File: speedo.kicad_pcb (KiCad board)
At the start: 4 copper layers, 70 x 34 mm, 52 parts, among them J1 Conn_01x08, J2 Conn_01x10, J3 Prog Header, Q1 BSS138, SW1 SW_Push, U1 US1881, U2 LT1762-3.3, U3 4N25, U4 LT1762-5, U5 ATMEGA328P-AU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

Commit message: Moved some pins around
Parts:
- renumbered REF** to REF1, REF** to REF2
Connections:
- U5 pad 1: BUTTON2 -> BUTTON1
- U5 pad 12: Net-(U5-Pad12) -> TACH
- U5 pad 2: TACH -> BUTTON2
- U5 pad 32: BUTTON1 -> HALL-EFF
- U5 pad 9: HALL-EFF -> Net-(U5-Pad9)
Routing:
- net HALL-EFF: track 56.0 -> 17.2 mm, vias 2 -> 0
- net BUTTON1: track 56.6 -> 60.1 mm
- net TACH: track 48.3 -> 45.3 mm
- net BUTTON2: track 60.7 -> 63.4 mm

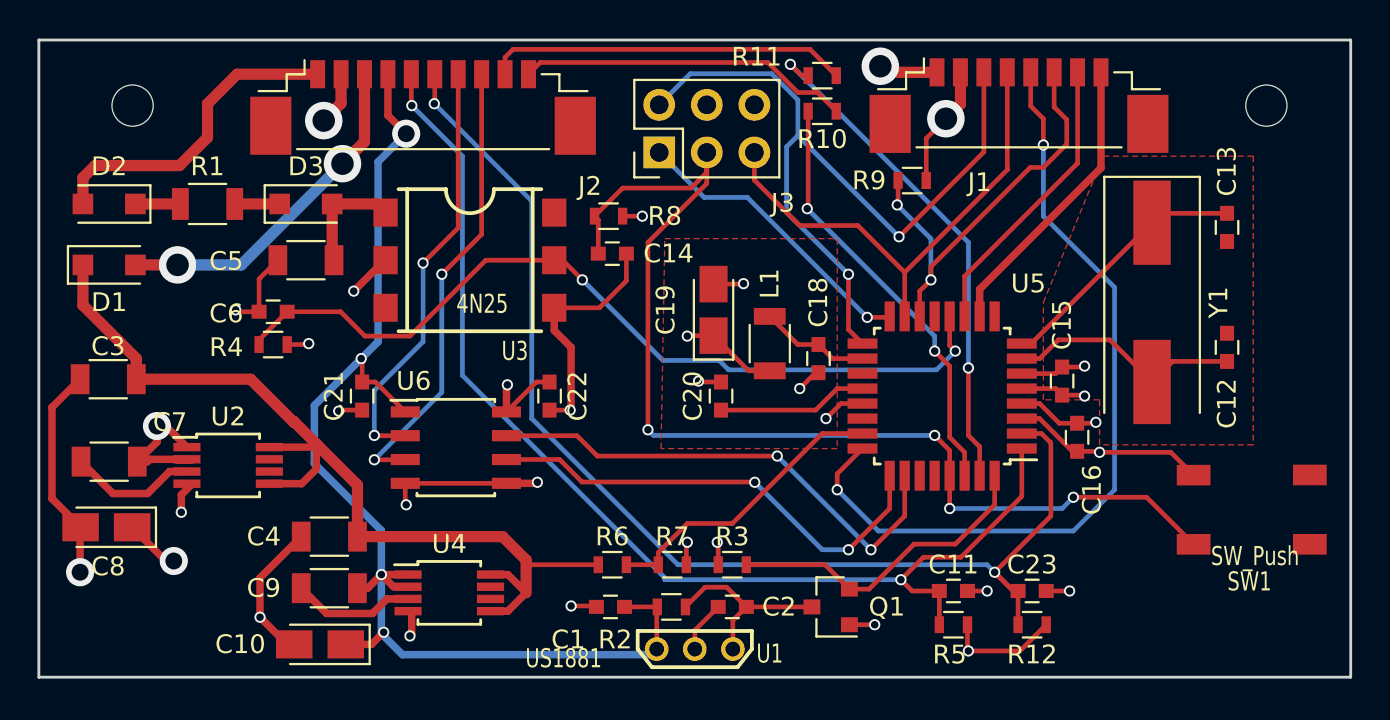
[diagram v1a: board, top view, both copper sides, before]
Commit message: Merged atmega644
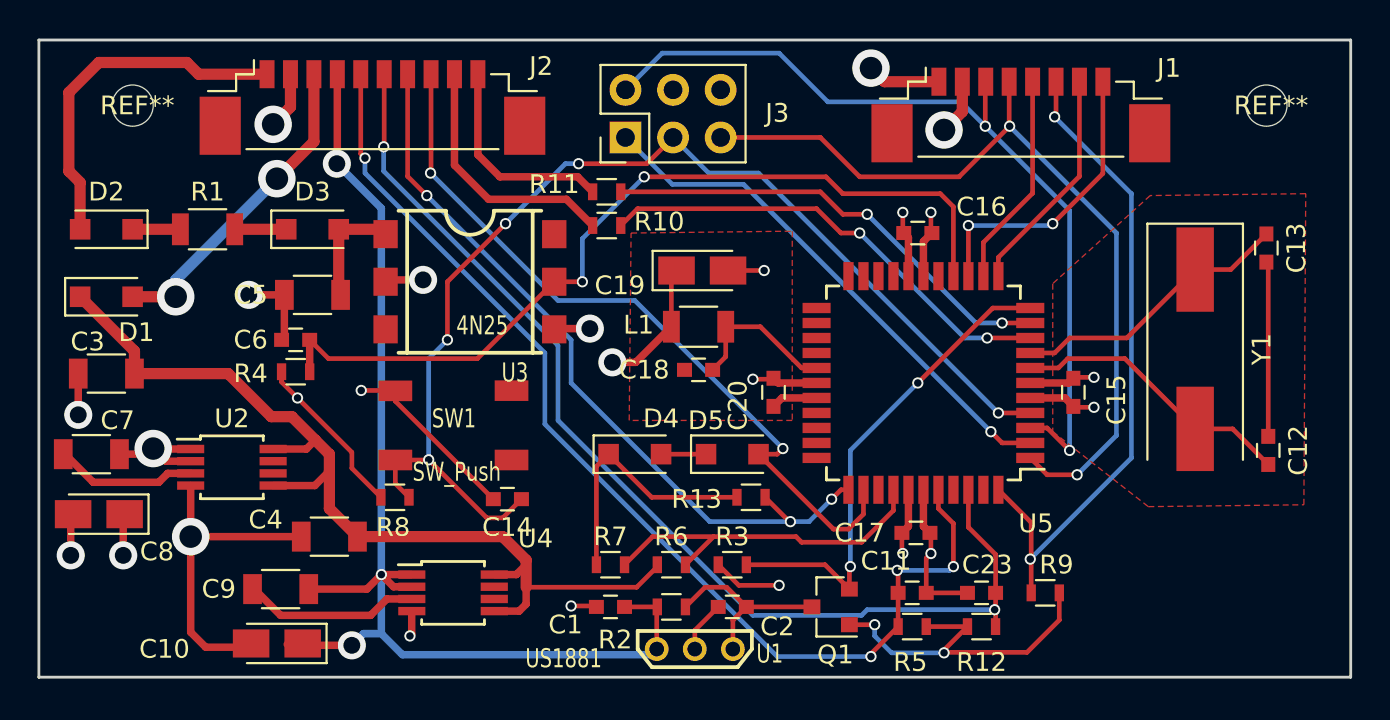
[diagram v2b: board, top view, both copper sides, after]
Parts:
- removed C21, C22: 100nF, Capacitors_SMD:C_0603
- removed U6: ADuM1200BR, Housings_SOIC:SOIC-8_3.9x4.9mm_Pitch1.27mm
- added C17: 100nF, Capacitors_SMD:C_0603, F.Cu at (146.8, 128.3)
- added D4: D, Diodes_SMD:D_SOD-123F, F.Cu at (131.8, 124.1)
- added D5: D, Diodes_SMD:D_SOD-123F, F.Cu at (137.0, 124.1)
- added R13: 18K, Resistors_SMD:R_0603, F.Cu at (138.0, 126.4)
- U5: value ATMEGA328P-AU -> ATMEGA644-20AU; footprint Housings_QFP:TQFP-32_7x7mm_Pitch0.8mm -> Housings_QFP:TQFP-44_10x10mm_Pitch0.8mm
- Y1: value 10MHz 18pF -> 16MHz 18pF
- moved SW1 42.8 mm to (122.4, 122.7)
- moved R9 23.1 mm to (153.7, 131.5)
- moved R8 18.8 mm to (119.0, 126.4), turned to 0 degrees
- moved C14 14.2 mm to (125.0, 126.5), turned to 180 degrees
- moved C16 13.8 mm to (146.9, 112.3), turned to 180 degrees
- moved R11 13.1 mm to (130.3, 110.1), turned to 0 degrees
- moved R10 13.0 mm to (130.3, 111.9), turned to 0 degrees
- moved C18 6.43 mm to (135.2, 119.6), turned to 180 degrees
- moved C12 5.92 mm to (165.6, 123.9)
- moved L1 3.91 mm to (135.2, 117.3), turned to 0 degrees
- moved Y1 3.40 mm to (161.7, 118.5)
- moved R7 3.30 mm to (130.5, 130.0), turned to 0 degrees
- moved R6 3.15 mm to (133.8, 130.0)
- moved C20 2.81 mm to (139.2, 120.8)
- moved R12 2.70 mm to (150.3, 133.3), turned to 0 degrees
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- renumbered REF2 to REF**, REF1 to REF**
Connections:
- net /xtal1 renamed Net-(C12-Pad2)
- net /xtal2 renamed Net-(C13-Pad2)
- J2 pad 10: RX -> TX
- J2 pad 7: GPIO1 -> LM35-POS
- J2 pad 8: GPIO2 -> LM35-NEG
- J2 pad 9: TX -> RX
- L1 pad 1: Net-(C18-Pad1) -> +3V3
- L1 pad 2: +3V3 -> Net-(C18-Pad1)
- U5 pad 1: BUTTON1 -> MOSI
- U5 pad 10: LCD-LED -> Net-(R11-Pad2)
- U5 pad 11: LCD-RST -> HALL-EFF
- U5 pad 12: TACH -> LCD-RST
- U5 pad 13: Net-(U5-Pad13) -> LCD-DC
- U5 pad 14: LCD-CS -> LCD-LED
- U5 pad 15: MOSI -> TACH
- U5 pad 16: MISO -> Net-(U5-Pad16)
- U5 pad 17: SCK -> +3V3
- U5 pad 18: Net-(C18-Pad1) -> GND
- U5 pad 2: BUTTON2 -> MISO
- U5 pad 20: Net-(C20-Pad1) -> Net-(U5-Pad20)
- U5 pad 21: GND -> Net-(U5-Pad21)
- U5 pad 23: VMEAS -> Net-(U5-Pad23)
- U5 pad 24: LCD-DC -> Net-(U5-Pad24)
- U5 pad 25: GPIO2-ISO -> Net-(U5-Pad25)
- U5 pad 26: GPIO1-ISO -> Net-(U5-Pad26)
- U5 pad 27: Net-(U5-Pad27) -> Net-(C18-Pad1)
- U5 pad 28: Net-(U5-Pad28) -> GND
- U5 pad 29: Reset -> Net-(C20-Pad1)
- U5 pad 3: GND -> SCK
- U5 pad 30: Net-(R10-Pad2) -> Net-(U5-Pad30)
- U5 pad 31: Net-(R11-Pad2) -> Net-(U5-Pad31)
- U5 pad 32: HALL-EFF -> Net-(U5-Pad32)
- U5 pad 4: +3V3 -> Reset
- U5 pad 5: GND -> +3V3
- U5 pad 6: +3V3 -> GND
- U5 pad 9: Net-(U5-Pad9) -> Net-(R10-Pad2)
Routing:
- net LM35-POS: track 0.00 -> 40.7 mm, vias 0 -> 3
- net LM35-NEG: track 0.00 -> 40.5 mm, vias 0 -> 2
- net LCD-DC: track 43.5 -> 11.5 mm, vias 2 -> 0
- net GPIO1-ISO: track 26.8 -> 0.00 mm, vias 2 -> 0
- net GPIO2-ISO: track 25.1 -> 0.00 mm, vias 2 -> 0
- net GPIO2: track 24.6 -> 0.00 mm, vias 2 -> 0
- net GPIO1: track 22.8 -> 0.00 mm, vias 2 -> 0
- net MOSI: track 26.9 -> 44.5 mm, vias 0 -> 2
- net +3V3: track 46.3 -> 61.1 mm, vias 12 -> 11
- net LCD-CS: track 22.9 -> 35.8 mm
- net MISO: track 16.0 -> 28.4 mm
- net GND: track 85.7 -> 96.2 mm, vias 22 -> 16
- net HALL-EFF: track 17.2 -> 26.2 mm, vias 0 -> 2
- net TX: track 19.3 -> 11.2 mm
- net Net-(C20-Pad1): track 8.03 -> 2.49 mm
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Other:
- rule pad_to_mask_clearance: 0.2 -> 0.0381
- board text added: "www.bit-builder.com-speedo-v2.0"
- board text removed: "www.bit-builder.com speedo - v2.0"

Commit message: Updated version of pcb due to clearance change
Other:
- board text added: "www.bit-builder.com-speedo-v2.1"
- board text removed: "www.bit-builder.com-speedo-v2.0"
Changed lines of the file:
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@@
   (title_block
     (title Speedo)
+    (rev 2.1)
   )
   (layers
@@
     )
   )
-  (gr_text www.bit-builder.com-speedo-v2.0 (at 149.1 134.2) (layer B.SilkS)
+  (gr_text www.bit-builder.com-speedo-v2.1 (at 149.1 134.2) (layer B.SilkS)
     (effects (font (size 1.5 1.5) (thickness 0.3)) (justify mirror))
   )

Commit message: Fixed ISP programmer and traces
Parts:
- J3: value Prog Header -> ISP
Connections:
- J3 pad 2: SCK -> Net-(J3-Pad2)
- J3 pad 3: Reset -> SCK
- J3 pad 4: GND -> MOSI
- J3 pad 5: MOSI -> Reset
- J3 pad 6: Net-(J3-Pad6) -> GND
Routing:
- net Reset: track 61.0 -> 66.9 mm
- net MOSI: track 44.5 -> 48.3 mm
- net SCK: track 45.8 -> 43.5 mm, vias 2 -> 3
